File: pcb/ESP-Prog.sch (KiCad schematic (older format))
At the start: 28 parts, among them J1 USB_B_Micro, Q1 MMSS8050-H-TP, Q2 MMSS8050-H-TP, SW1 SW_DIP_x01, SW2 SW_DIP_x01, U1 LD1117S33TR_SOT223

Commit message: primer versión terminada del esquemático
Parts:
- removed C? (x2): C, symbol Device:C
- removed J?: Conn_02x05_Odd_Even, symbol Connector_Generic:Conn_02x05_Odd_Even
- removed J?: Conn_02x03_Odd_Even, symbol Connector_Generic:Conn_02x03_Odd_Even
- added D7, D8, D9: D_TVS, symbol Device:D_TVS
- gave numbers to parts that had none: 7
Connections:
- net labels added: +3.3V, ESP_IO0, ESP_RXD0, ESP_TCK, ESP_TDI, ESP_TDO, ESP_TMS, ESP_TXD0, USB_DM, USB_DP, VDD, VDDA
- net labels removed: VDD_J
- wire segments 111 -> 101
- no-connect marks 2 -> 3
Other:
- moved on the sheet: J2, J4, J5

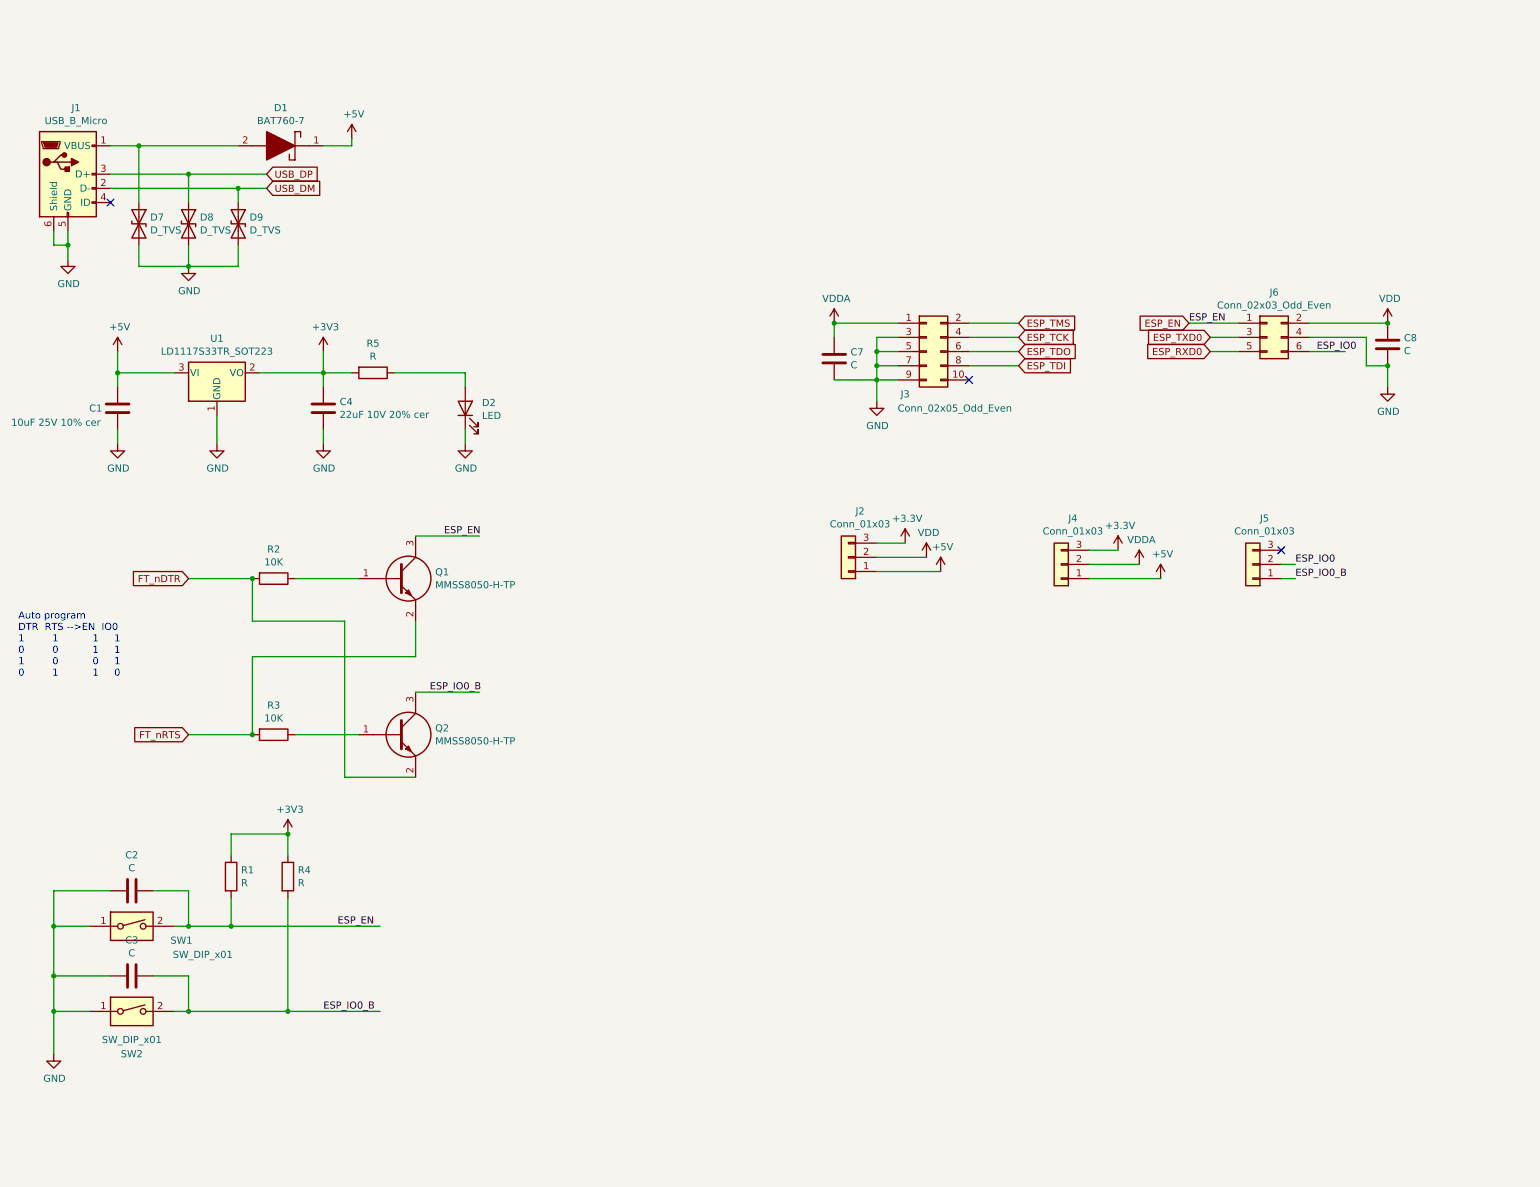
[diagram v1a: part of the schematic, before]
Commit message: - se agregan todos los footprints
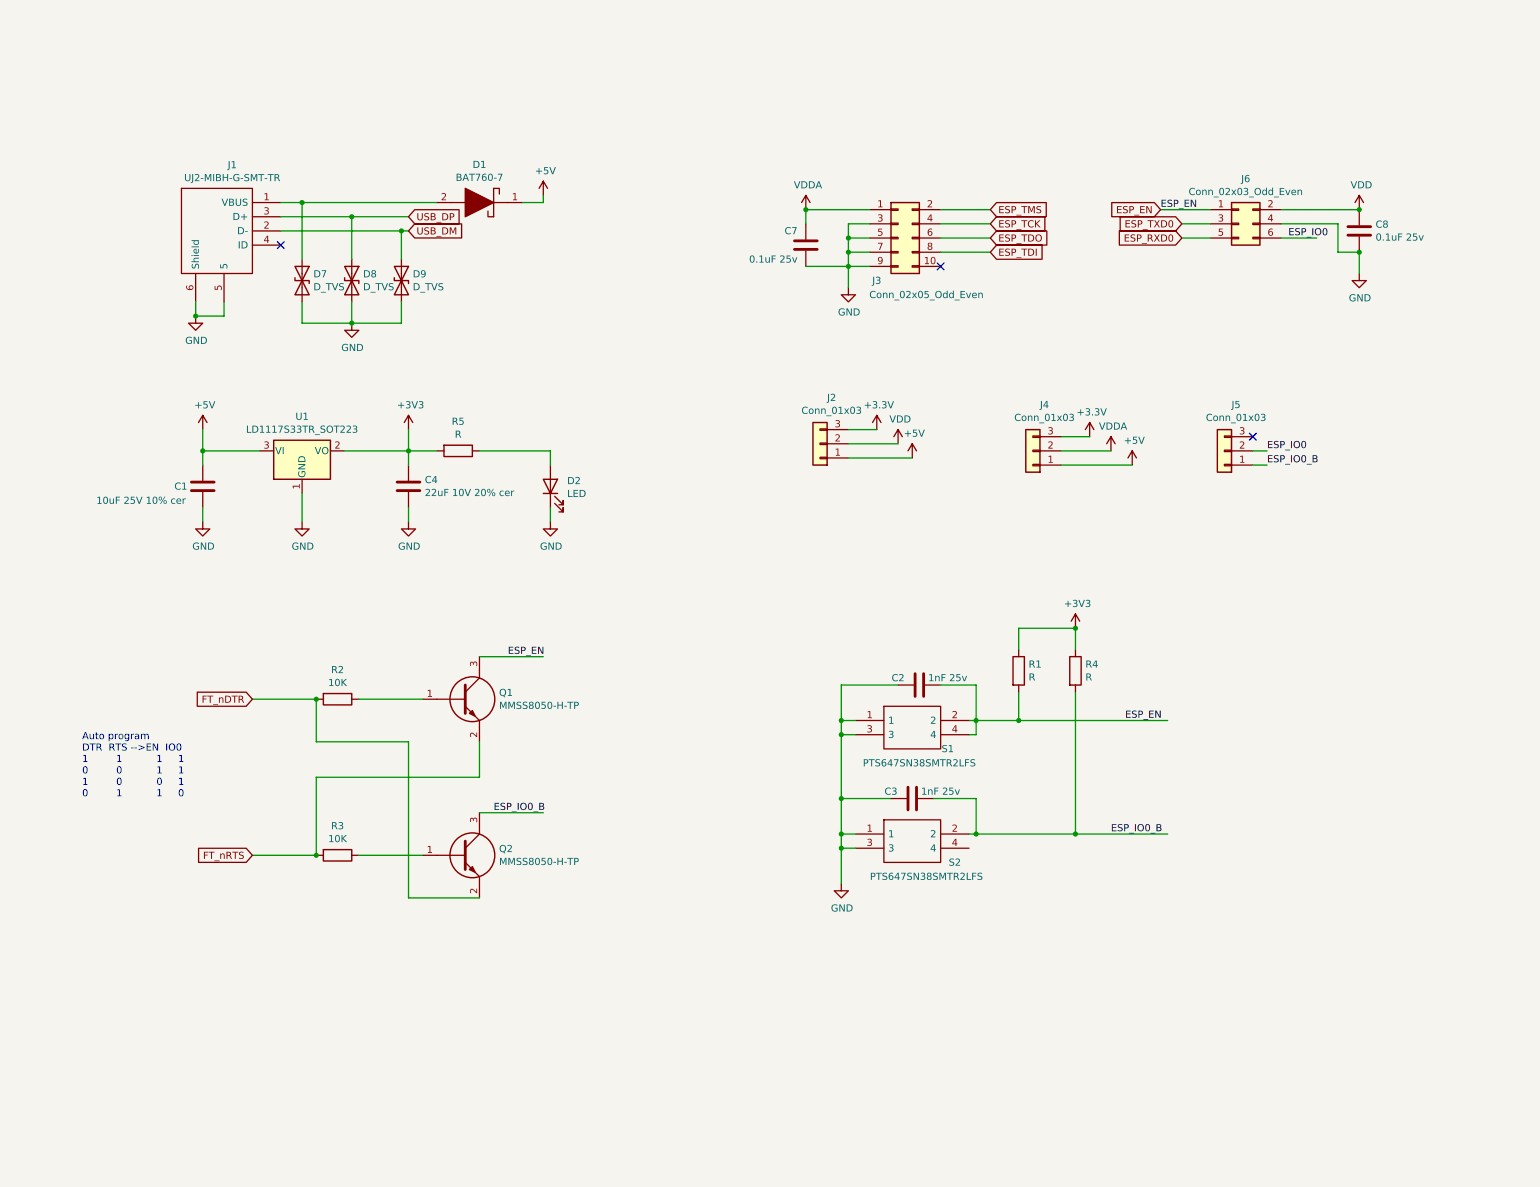
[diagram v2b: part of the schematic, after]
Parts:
- removed J1: USB_B_Micro, symbol Connector:USB_B_Micro
- removed SW1, SW2: SW_DIP_x01, symbol Switch:SW_DIP_x01
- added J1: UJ2-MIBH-G-SMT-TR, SamacSys_Parts:UJ2MIBHGSMTTR, symbol SamacSys_Parts:UJ2-MIBH-G-SMT-TR
- added S1, S2: PTS647SN38SMTR2LFS, SamacSys_Parts:PTS647SM38SMTR2LFS, symbol SamacSys_Parts:PTS647SN38SMTR2LFS
- C1, C4: footprint (none) -> Capacitor_SMD:C_0603_1608Metric
- C2, C3: value C -> 1nF 25v; footprint (none) -> Capacitor_SMD:C_0603_1608Metric
- C7, C8: value C -> 0.1uF 25v; footprint (none) -> Capacitor_SMD:C_0603_1608Metric
- D1: footprint SOD2513X120N -> Diode_SMD:D_SOD-323
- D2: footprint (none) -> LED_SMD:LED_0603_1608Metric
- D7, D8, D9: footprint (none) -> Diode_SMD:D_SOD-523
- J2, J4, J5: footprint (none) -> Connector_PinHeader_2.54mm:PinHeader_1x03_P2.54mm_Vertical
- J3, J6: footprint (none) -> Connector_PinHeader_1.27mm:PinHeader_2x05_P1.27mm_Vertical_SMD
- Q1, Q2: footprint SI2305TP -> SamacSys_Parts:SI2305TP
- R1, R2, R3, R4, R5: footprint (none) -> Resistor_SMD:R_0603_1608Metric
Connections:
- wire segments 101 -> 106
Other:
- moved on the sheet: C1, C2, C3, C4, C7, C8, D1, D2, D7, D8, D9, J2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
